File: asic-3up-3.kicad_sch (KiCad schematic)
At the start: 89 parts, among them J10 Conn_01x01, J11 Conn_01x01, J21 Conn_01x01, J22 Conn_01x01, U4 SN74AVC4T774, U5 25MHz, U66 MCP1824T-1202E/OT, U67 MCP1824T-1202E/OT, U68 MCP1824T-1202E/OT, U69 MCP1824T-0802E, U70 MCP1824T-0802E, U71 MCP1824T-0802E, U72 BM1362AC_MODE1, U73 BM1362AC_MODE0, U74 BM1362AC_MODE1

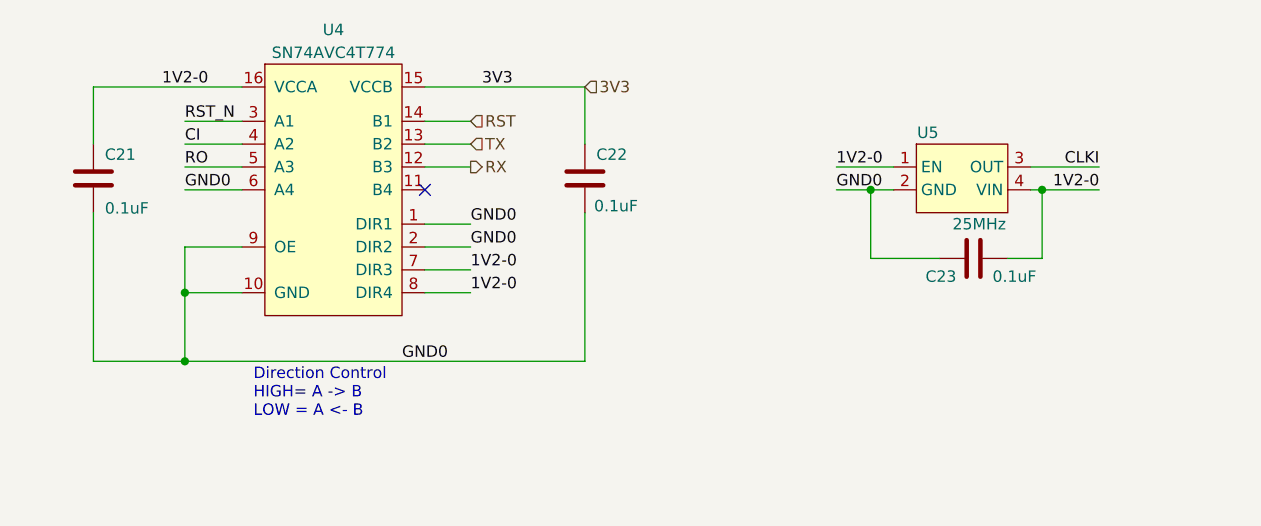
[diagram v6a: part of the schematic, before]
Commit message: placements done. shrunk test points
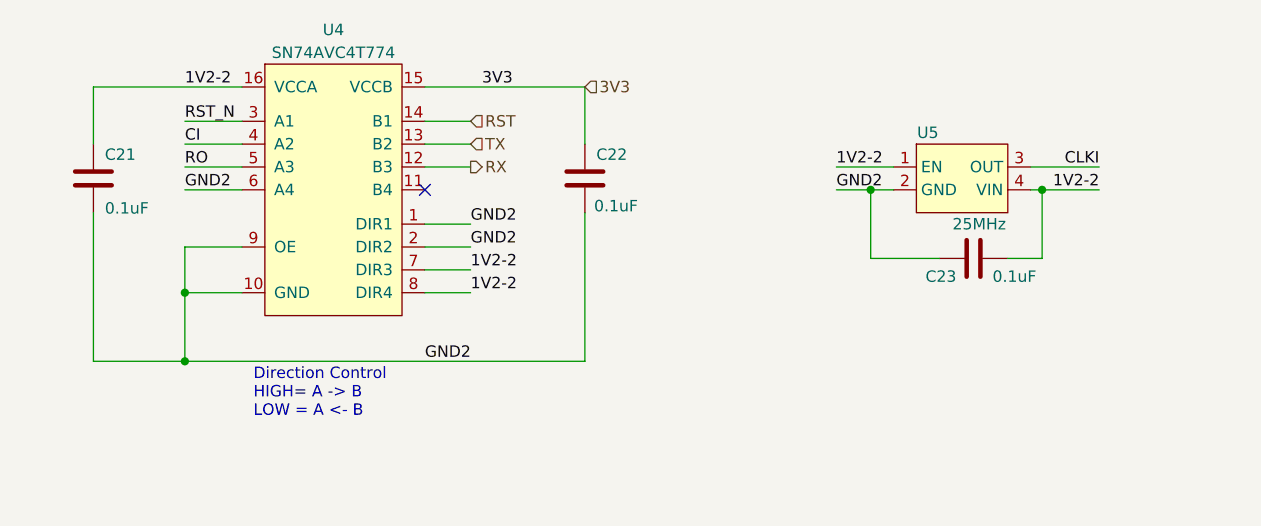
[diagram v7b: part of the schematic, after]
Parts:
- TP1, TP142, TP143, TP144, TP145, TP146, TP147, TP148, TP149, TP150, TP151, TP152, TP153, TP154, TP155, TP156, TP157, TP2, TP3, TP4, TP5, TP6, TP7, TP8, TP9: footprint TestPoint:TestPoint_Pad_D1.5mm -> TestPoint:TestPoint_Pad_D1.0mm
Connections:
- net 1V2-0: no longer C21.1, C23.2, U4.16 (VCCA), U4.7 (DIR3), U4.8 (DIR4), U5.1 (EN), U5.4 (VIN)
- net 1V2-2: now also C21.1, C23.2, U4.16 (VCCA), U4.7 (DIR3), U4.8 (DIR4), U5.1 (EN), U5.4 (VIN)
- net GND0: no longer C21.2, C22.2, C23.1, U4.1 (DIR1), U4.10 (GND), U4.2 (DIR2), U4.6 (A4), U4.9 (OE), U5.2 (GND)
- net VSS: now also C21.2, C22.2, C23.1, U4.1 (DIR1), U4.10 (GND), U4.2 (DIR2), U4.6 (A4), U4.9 (OE), U5.2 (GND)
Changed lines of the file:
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@@
 		)
 	)
-	(label "1V2-0"
-		(at 105.41 57.15 0)
-		(fields_autoplaced yes)
-		(effects
-			(font
-				(size 1.27 1.27)
-			)
-			(justify left bottom)
-		)
-	)
 	(label "CLKI"
 		(at 175.26 43.18 180)
@@
 		)
 	)
-	(label "GND0"
-		(at 105.41 52.07 0)
-		(fields_autoplaced yes)
-		(effects
-			(font
-				(size 1.27 1.27)
-			)
-			(justify left bottom)
-		)
-	)
 	(label "CI"
 		(at 219.71 222.25 0)
@@
 		)
 	)
-	(label "0V8-1"
-		(at 154.94 163.83 0)
+	(label "GND2"
+		(at 73.66 45.72 0)
 		(fields_autoplaced yes)
 		(effects
@@
 		)
 	)
-	(label "GND0"
-		(at 146.05 45.72 0)
+	(label "0V8-1"
+		(at 154.94 163.83 0)
 		(fields_autoplaced yes)
 		(effects
@@
 	)
 	(label "1V2-2"
+		(at 73.66 34.29 0)
+		(fields_autoplaced yes)
+		(effects
+			(font
+				(size 1.27 1.27)
+			)
+			(justify left bottom)
+		)
+	)
+	(label "1V2-2"
 		(at 222.25 237.49 0)
 		(fields_autoplaced yes)
@@
 		)
 	)
+	(label "1V2-2"
+		(at 105.41 57.15 0)
+		(fields_autoplaced yes)
+		(effects
+			(font
+				(size 1.27 1.27)
+			)
+			(justify left bottom)
+		)
+	)
 	(label "GND0"
 		(at 78.74 119.38 0)
@@
 		)
 	)
-	(label "GND1"
-		(at 255.27 199.39 0)
+	(label "GND2"
+		(at 146.05 45.72 0)
 		(fields_autoplaced yes)
 		(effects
@@
 		)
 	)
-	(label "RO"
-		(at 73.66 43.18 0)
+	(label "GND1"
+		(at 255.27 199.39 0)
 		(fields_autoplaced yes)
 		(effects
@@
 		)
 	)
-	(label "GND0"
-		(at 254 143.51 0)
+	(label "RO"
+		(at 73.66 43.18 0)
 		(fields_autoplaced yes)
 		(effects
@@
 	)
 	(label "GND0"
-		(at 105.41 49.53 0)
+		(at 254 143.51 0)
 		(fields_autoplaced yes)
 		(effects
@@
 		)
 	)
-	(label "1V2-0"
+	(label "1V2-2"
 		(at 175.26 45.72 180)
 		(fields_autoplaced yes)
@@
 	)
 	(label "GND0"
-		(at 97.79 64.77 0)
-		(fields_autoplaced yes)
-		(effects
-			(font
-				(size 1.27 1.27)
-			)
-			(justify left bottom)
-		)
-	)
-	(label "GND0"
 		(at 350.52 119.38 0)
 		(fields_autoplaced yes)
@@
 		)
 	)
-	(label "1V2-0"
-		(at 105.41 54.61 0)
+	(label "GND0"
+		(at 185.42 130.81 180)
 		(fields_autoplaced yes)
 		(effects
@@
 				(size 1.27 1.27)
 			)
-			(justify left bottom)
+			(justify right bottom)
 		)
 	)
-	(label "GND0"
-		(at 185.42 130.81 180)
+	(label "GND2"
+		(at 105.41 49.53 0)
 		(fields_autoplaced yes)
 		(effects
@@
 				(size 1.27 1.27)
 			)
-			(justify right bottom)
+			(justify left bottom)
 		)
 	)
@@
 		)
 	)
+	(label "1V2-2"
+		(at 105.41 54.61 0)
+		(fields_autoplaced yes)
+		(effects
+			(font
+				(size 1.27 1.27)
+			)
+			(justify left bottom)
+		)
+	)
+	(label "1V2-2"
+		(at 146.05 43.18 0)
+		(fields_autoplaced yes)
+		(effects
+			(font
+				(size 1.27 1.27)
+			)
+			(justify left bottom)
+		)
+	)
 	(label "RST_N"
 		(at 73.66 38.1 0)
@@
 		)
 	)
-	(label "GND0"
-		(at 73.66 45.72 0)
+	(label "GND2"
+		(at 105.41 52.07 0)
 		(fields_autoplaced yes)
 		(effects
@@
 		)
 	)
-	(label "1V2-0"
-		(at 71.12 34.29 0)
+	(label "GND0"
+		(at 306.07 133.35 0)
 		(fields_autoplaced yes)
 		(effects
@@
 		)
 	)
-	(label "GND0"
-		(at 306.07 133.35 0)
+	(label "1V2-0"
+		(at 222.25 125.73 0)
 		(fields_autoplaced yes)
 		(effects
@@
 		)
 	)
-	(label "1V2-0"
-		(at 222.25 125.73 0)
+	(label "GND2"
+		(at 100.33 64.77 0)
 		(fields_autoplaced yes)
 		(effects
@@
 		)
 	)
-	(label "1V2-0"
-		(at 146.05 43.18 0)
-		(fields_autoplaced yes)
-		(effects
-			(font
-				(size 1.27 1.27)
-			)
-			(justify left bottom)
-		)
-	)
 	(hierarchical_label "TX"
 		(shape input)
@@
 			)
 		)
-		(property "Footprint" "TestPoint:TestPoint_Pad_D1.5mm"
+		(property "Footprint" "TestPoint:TestPoint_Pad_D1.0mm"
 			(at 160.02 215.9 0)
 			(effects
@@
 			)
 		)
-		(property "Footprint" "TestPoint:TestPoint_Pad_D1.5mm"
+		(property "Footprint" "TestPoint:TestPoint_Pad_D1.0mm"
 			(at 160.02 158.75 0)
 			(effects
@@
 			)
 		)
-		(property "Footprint" "TestPoint:TestPoint_Pad_D1.5mm"
+		(property "Footprint" "TestPoint:TestPoint_Pad_D1.0mm"
 			(at 307.34 115.57 0)
 			(effects
@@
 			)
 		)
-		(property "Footprint" "TestPoint:TestPoint_Pad_D1.5mm"
+		(property "Footprint" "TestPoint:TestPoint_Pad_D1.0mm"
 			(at 307.34 110.49 0)
 			(effects
@@
 			)
 		)
-		(property "Footprint" "TestPoint:TestPoint_Pad_D1.5mm"
+		(property "Footprint" "TestPoint:TestPoint_Pad_D1.0mm"
 			(at 313.69 161.29 0)
 			(effects
@@
 			)
 		)
-		(property "Footprint" "TestPoint:TestPoint_Pad_D1.5mm"
+		(property "Footprint" "TestPoint:TestPoint_Pad_D1.0mm"
 			(at 181.61 105.41 0)
 			(effects
@@
 			)
 		)
-		(property "Footprint" "TestPoint:TestPoint_Pad_D1.5mm"
+		(property "Footprint" "TestPoint:TestPoint_Pad_D1.0mm"
 			(at 307.34 105.41 0)
 			(effects
@@
 			)
 		)
-		(property "Footprint" "TestPoint:TestPoint_Pad_D1.5mm"
+		(property "Footprint" "TestPoint:TestPoint_Pad_D1.0mm"
 			(at 313.69 171.45 0)
 			(effects
@@
 			)
 		)
-		(property "Footprint" "TestPoint:TestPoint_Pad_D1.5mm"
+		(property "Footprint" "TestPoint:TestPoint_Pad_D1.0mm"
 			(at 313.69 163.83 0)
 			(effects
@@
 			)
 		)
-		(property "Footprint" "TestPoint:TestPoint_Pad_D1.5mm"
+		(property "Footprint" "TestPoint:TestPoint_Pad_D1.0mm"
 			(at 313.69 166.37 0)
 			(effects
@@
 			)
 		)
-		(property "Footprint" "TestPoint:TestPoint_Pad_D1.5mm"
+		(property "Footprint" "TestPoint:TestPoint_Pad_D1.0mm"
 			(at 307.34 113.03 0)
 			(effects
@@
 			)
 		)
-		(property "Footprint" "TestPoint:TestPoint_Pad_D1.5mm"
+		(property "Footprint" "TestPoint:TestPoint_Pad_D1.0mm"
 			(at 307.34 107.95 0)
 			(effects
@@
 			)
 		)
-		(property "Footprint" "TestPoint:TestPoint_Pad_D1.5mm"
+		(property "Footprint" "TestPoint:TestPoint_Pad_D1.0mm"
 			(at 100.33 158.75 0)
 			(effects
@@
 			)
 		)
-		(property "Footprint" "TestPoint:TestPoint_Pad_D1.5mm"
+		(property "Footprint" "TestPoint:TestPoint_Pad_D1.0mm"
 			(at 313.69 168.91 0)
 			(effects
@@
 			)
 		)
-		(property "Footprint" "TestPoint:TestPoint_Pad_D1.5mm"
+		(property "Footprint" "TestPoint:TestPoint_Pad_D1.0mm"
 			(at 219.71 217.17 0)
 			(effects
@@
 			)
 		)
-		(property "Footprint" "TestPoint:TestPoint_Pad_D1.5mm"
+		(property "Footprint" "TestPoint:TestPoint_Pad_D1.0mm"
 			(at 219.71 212.09 0)
 			(effects
@@
 			)
 		)
-		(property "Footprint" "TestPoint:TestPoint_Pad_D1.5mm"
+		(property "Footprint" "TestPoint:TestPoint_Pad_D1.0mm"
 			(at 219.71 214.63 0)
 			(effects
@@
 			)
 		)
-		(property "Footprint" "TestPoint:TestPoint_Pad_D1.5mm"
+		(property "Footprint" "TestPoint:TestPoint_Pad_D1.0mm"
 			(at 100.33 100.33 0)
 			(effects
@@
 			)
 		)
-		(property "Footprint" "TestPoint:TestPoint_Pad_D1.5mm"
+		(property "Footprint" "TestPoint:TestPoint_Pad_D1.0mm"
 			(at 219.71 207.01 0)
 			(effects
@@
 			)
 		)
-		(property "Footprint" "TestPoint:TestPoint_Pad_D1.5mm"
+		(property "Footprint" "TestPoint:TestPoint_Pad_D1.0mm"
 			(at 160.02 100.33 0)
 			(effects
@@
 			)
 		)
-		(property "Footprint" "TestPoint:TestPoint_Pad_D1.5mm"
+		(property "Footprint" "TestPoint:TestPoint_Pad_D1.0mm"
 			(at 100.33 215.9 0)
 			(effects
@@
 			)
 		)
-		(property "Footprint" "TestPoint:TestPoint_Pad_D1.5mm"
+		(property "Footprint" "TestPoint:TestPoint_Pad_D1.0mm"
 			(at 181.61 110.49 0)
 			(effects
@@
 			)
 		)
-		(property "Footprint" "TestPoint:TestPoint_Pad_D1.5mm"
+		(property "Footprint" "TestPoint:TestPoint_Pad_D1.0mm"
 			(at 181.61 107.95 0)
 			(effects
@@
 			)
 		)
-		(property "Footprint" "TestPoint:TestPoint_Pad_D1.5mm"
+		(property "Footprint" "TestPoint:TestPoint_Pad_D1.0mm"
 			(at 181.61 113.03 0)
 			(effects
@@
 			)
 		)
-		(property "Footprint" "TestPoint:TestPoint_Pad_D1.5mm"
+		(property "Footprint" "TestPoint:TestPoint_Pad_D1.0mm"
 			(at 181.61 115.57 0)
 			(effects

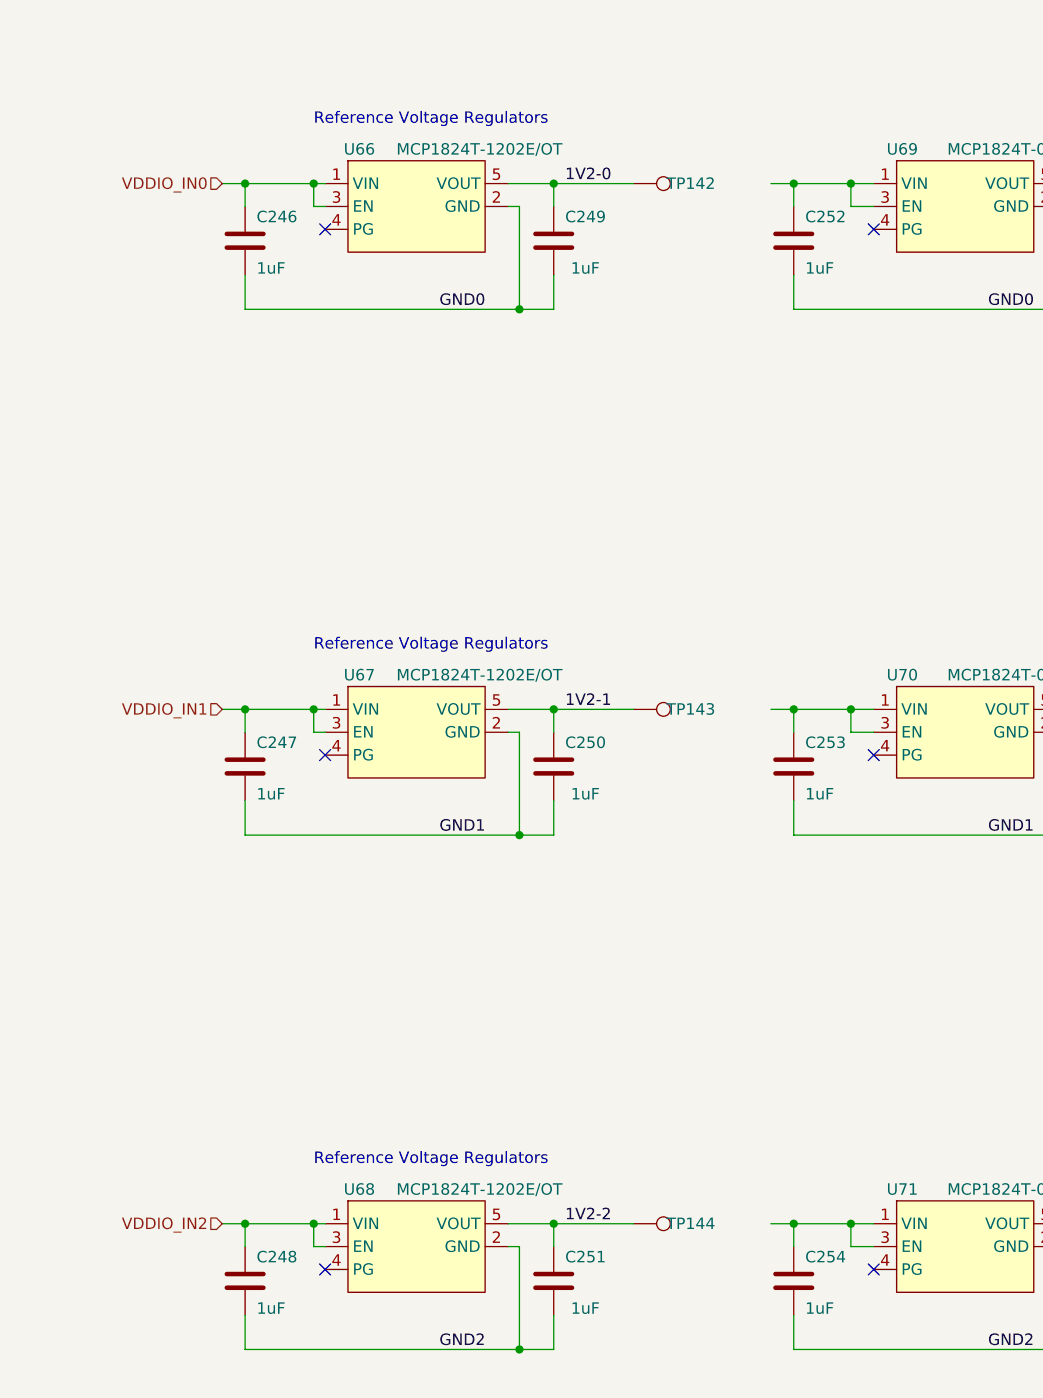
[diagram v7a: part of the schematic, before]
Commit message: added temp sensors. wired up (hopeful) vreg EN circuit. lots of LDO routing.
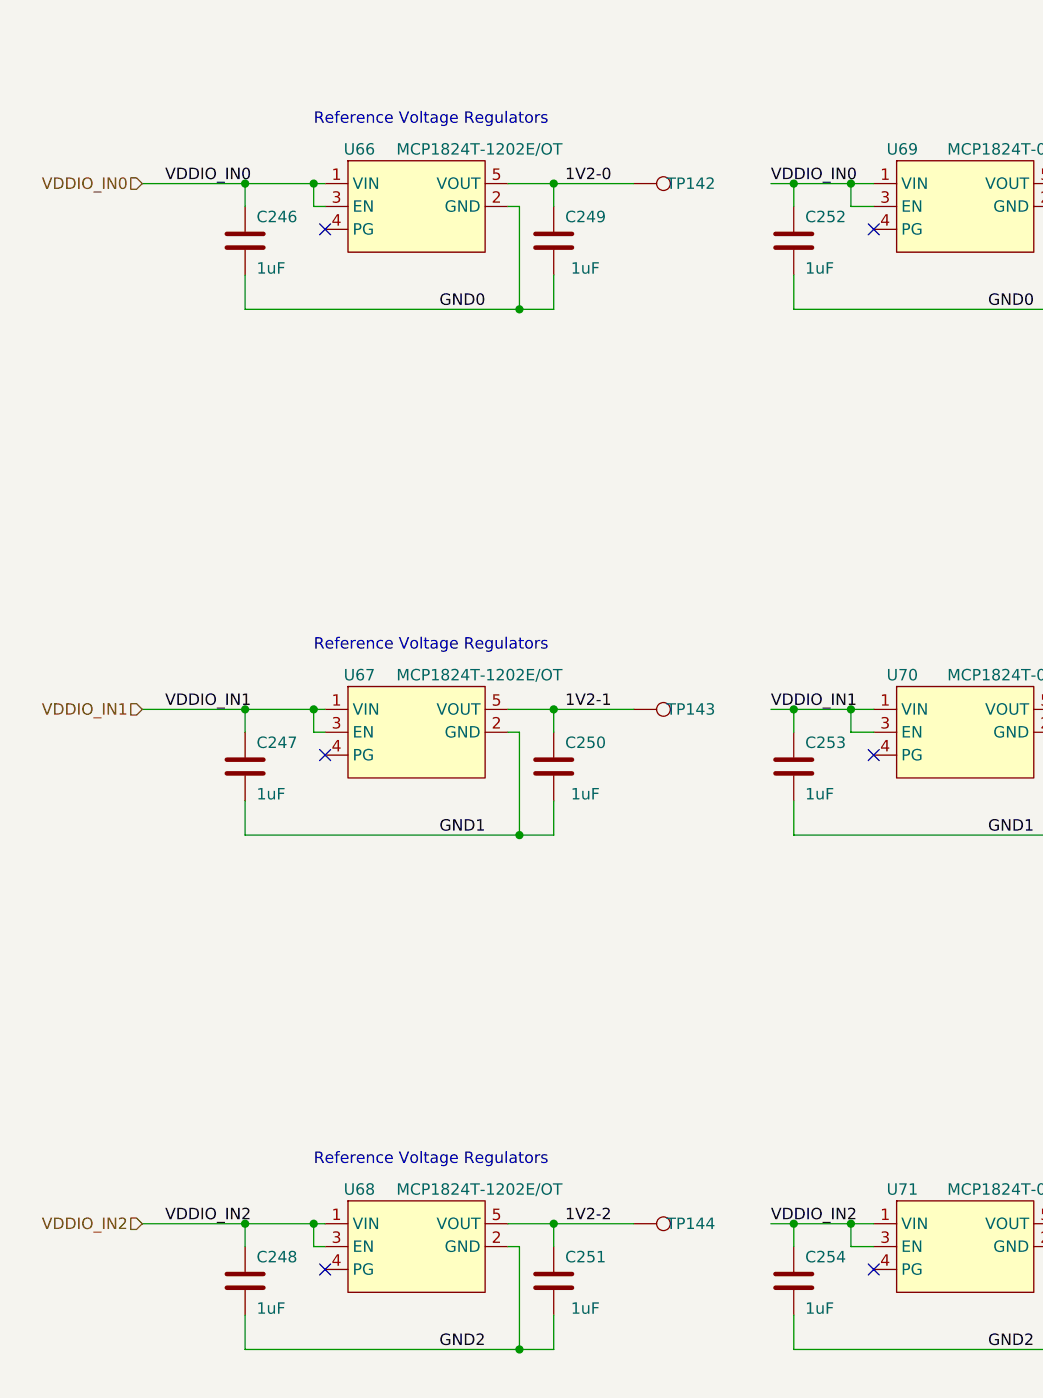
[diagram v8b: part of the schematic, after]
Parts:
- J21: footprint emberone:5x9_powertab -> emberone:14x9_powertab_L
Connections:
- net VDDIO_IN0: now also C252.1, U69.1 (VIN), U69.3 (EN)
- net VDDIO_IN1: now also C253.1, U70.1 (VIN), U70.3 (EN)
- net VDDIO_IN2: now also C254.1, U71.1 (VIN), U71.3 (EN)
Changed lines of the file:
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@@
 	(wire
 		(pts
-			(xy 54.61 163.83) (xy 57.15 163.83)
+			(xy 45.72 163.83) (xy 57.15 163.83)
 		)
 		(stroke
@@
 	(wire
 		(pts
-			(xy 54.61 105.41) (xy 57.15 105.41)
+			(xy 45.72 105.41) (xy 57.15 105.41)
 		)
 		(stroke
@@
 	(wire
 		(pts
-			(xy 54.61 220.98) (xy 57.15 220.98)
+			(xy 45.72 220.98) (xy 57.15 220.98)
 		)
 		(stroke
@@
 		)
 	)
+	(label "VDDIO_IN0"
+		(at 48.26 105.41 0)
+		(fields_autoplaced yes)
+		(effects
+			(font
+				(size 1.27 1.27)
+			)
+			(justify left bottom)
+		)
+	)
 	(label "RO"
 		(at 73.66 43.18 0)
@@
 		)
 	)
+	(label "VDDIO_IN2"
+		(at 48.26 220.98 0)
+		(fields_autoplaced yes)
+		(effects
+			(font
+				(size 1.27 1.27)
+			)
+			(justify left bottom)
+		)
+	)
 	(label "GND0"
 		(at 185.42 130.81 180)
@@
 		)
 	)
+	(label "VDDIO_IN1"
+		(at 48.26 163.83 0)
+		(fields_autoplaced yes)
+		(effects
+			(font
+				(size 1.27 1.27)
+			)
+			(justify left bottom)
+		)
+	)
 	(label "GND1"
 		(at 139.7 177.8 0)
@@
 		)
 	)
+	(label "VDDIO_IN1"
+		(at 115.57 163.83 0)
+		(fields_autoplaced yes)
+		(effects
+			(font
+				(size 1.27 1.27)
+			)
+			(justify left bottom)
+		)
+	)
 	(label "GND0"
 		(at 306.07 133.35 0)
@@
 		)
 	)
+	(label "VDDIO_IN0"
+		(at 115.57 105.41 0)
+		(fields_autoplaced yes)
+		(effects
+			(font
+				(size 1.27 1.27)
+			)
+			(justify left bottom)
+		)
+	)
+	(label "VDDIO_IN2"
+		(at 115.57 220.98 0)
+		(fields_autoplaced yes)
+		(effects
+			(font
+				(size 1.27 1.27)
+			)
+			(justify left bottom)
+		)
+	)
 	(label "GND2"
 		(at 100.33 64.77 0)
@@
 	(hierarchical_label "VDDIO_IN0"
 		(shape input)
-		(at 54.61 105.41 180)
+		(at 45.72 105.41 180)
 		(fields_autoplaced yes)
 		(effects
@@
 	(hierarchical_label "VDDIO_IN1"
 		(shape input)
-		(at 54.61 163.83 180)
+		(at 45.72 163.83 180)
 		(fields_autoplaced yes)
 		(effects
@@
 	(hierarchical_label "VDDIO_IN2"
 		(shape input)
-		(at 54.61 220.98 180)
+		(at 45.72 220.98 180)
 		(fields_autoplaced yes)
 		(effects
@@
 			)
 		)
-		(property "Footprint" "emberone:5x9_powertab"
+		(property "Footprint" "emberone:14x9_powertab_L"
 			(at 254 250.19 0)
 			(effects
